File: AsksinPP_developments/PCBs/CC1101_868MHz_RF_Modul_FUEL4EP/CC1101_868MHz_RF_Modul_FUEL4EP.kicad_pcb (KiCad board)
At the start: 2 copper layers, 19 x 13 mm, 39 parts, among them U1 CC1101RGPR, Y1 Crystal 26MHz

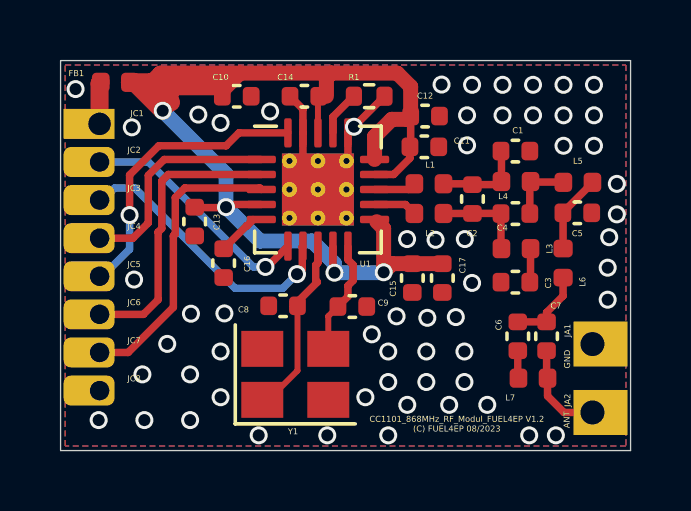
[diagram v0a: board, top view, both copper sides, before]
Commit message: PCBs: CC1101_868MHz_RF_Modul_FUEL4EP, CC1101_868MHz_UFL_RF_Modul_FUEL4EP: update of silkscreen texts
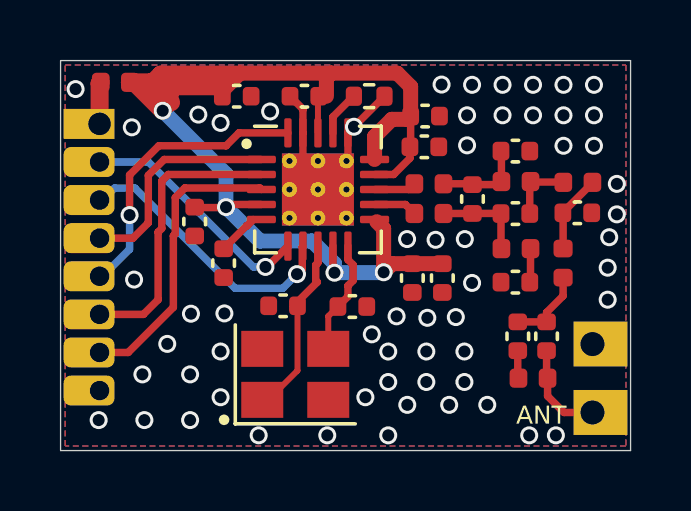
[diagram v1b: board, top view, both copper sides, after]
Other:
- board text added: "CC1101_868MHz_ RF_Modul_FUEL4EP V1.3 (C) FUEL4EP 09/2023"
- board text added: "JLCJLCJLCJLC"
- board text removed: "CC1101_868MHz_RF_Modul_FUEL4EP V1.2 (C) FUEL4EP 08/2023"
- board text removed: "GND"

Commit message: PCBs: CC1101_868MHz_RF_Modul_FUEL4EP: more GND vias added; doc updates
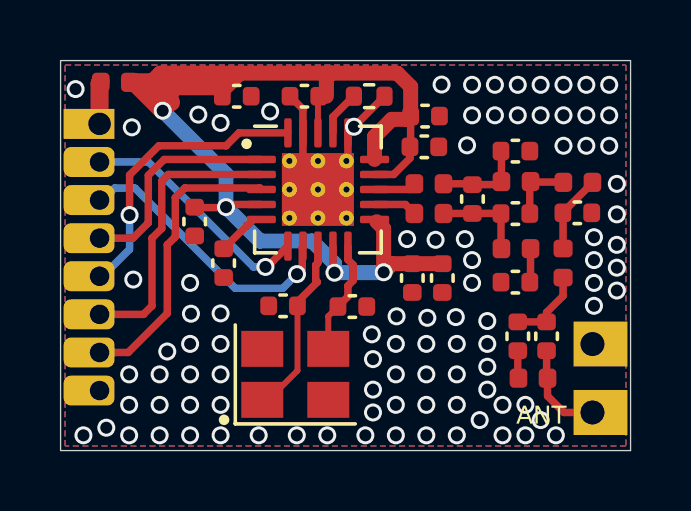
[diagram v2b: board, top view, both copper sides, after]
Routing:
- net GND: vias 59 -> 94
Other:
- board text added: "CC1101_868MHz_ RF_Modul_FUEL4EP V1.4 (C) FUEL4EP 09/2023"
- board text removed: "CC1101_868MHz_ RF_Modul_FUEL4EP V1.3 (C) FUEL4EP 09/2023"

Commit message: PCBs: CC1101_868MHz_RF_Modul_FUEL4EP: Improved decoupling by shorter return paths for GND loops
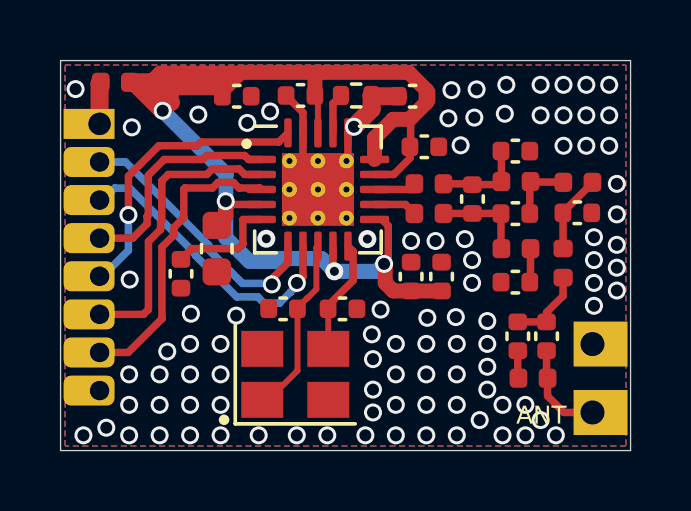
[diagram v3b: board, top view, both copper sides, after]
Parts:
- C13: footprint Capacitor_SMD:C_0402_1005Metric -> Capacitor_SMD:C_0603_1608Metric
- moved C16 1.47 mm to (4.01, -5.89)
- moved C13 1.17 mm to (5.21, -6.73)
- moved C12 0.78 mm to (11.7, -11.8), turned to 180 degrees
- moved R1 0.43 mm to (9.86, -11.8)
- moved C9 0.34 mm to (9.40, -4.72)
- moved C14 0.13 mm to (8.00, -11.8)
- moved C8 0.10 mm to (7.42, -4.72)
- moved C15 0.07 mm to (11.7, -5.80), turned to 90 degrees
- moved C17 0.06 mm to (12.7, -5.80), turned to 90 degrees
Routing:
- net Net-(C16-Pad1): track 1.40 -> 3.71 mm
- net VDDA: track 43.6 -> 45.3 mm
- net /GDO0: track 7.92 -> 8.78 mm
- net GND: track 5.01 -> 5.83 mm
- net /~{CS}: track 9.24 -> 9.82 mm
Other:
- board text added: "CC1101_868MHz_ RF_Modul_FUEL4EP V1.5 (C) FUEL4EP 09/2023"
- board text removed: "CC1101_868MHz_ RF_Modul_FUEL4EP V1.4 (C) FUEL4EP 09/2023"

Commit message: PCBs: CC1101_868MHz_RF_Modul_FUEL4EP and CC1101_868MHz_UFL_RF_Modul_FUEL4EP: Reduction of parasitic capaitance of oscillator layout; use 1% CoG capacitors for oscillator
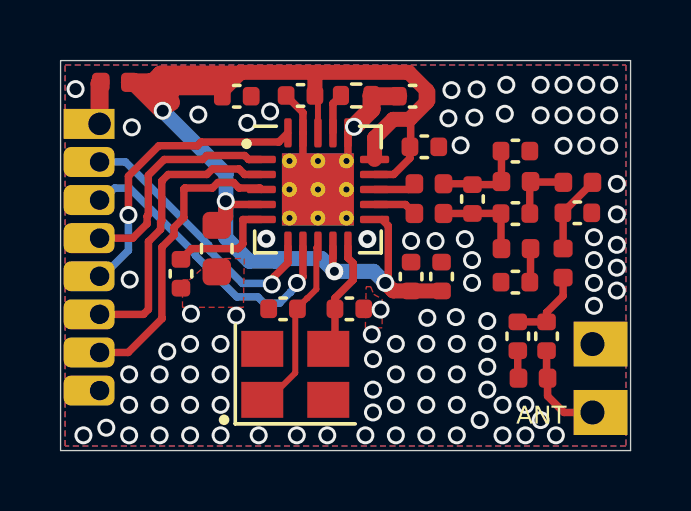
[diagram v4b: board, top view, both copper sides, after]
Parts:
- moved C9 0.23 mm to (9.63, -4.72)
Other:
- board text added: "CC1101_868MHz_ RF_Modul_FUEL4EP V1.6 (C) FUEL4EP 09/2023"
- board text removed: "CC1101_868MHz_ RF_Modul_FUEL4EP V1.5 (C) FUEL4EP 09/2023"
